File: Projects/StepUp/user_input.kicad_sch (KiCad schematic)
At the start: 10 parts, among them J12 Conn_02x03_Odd_Even

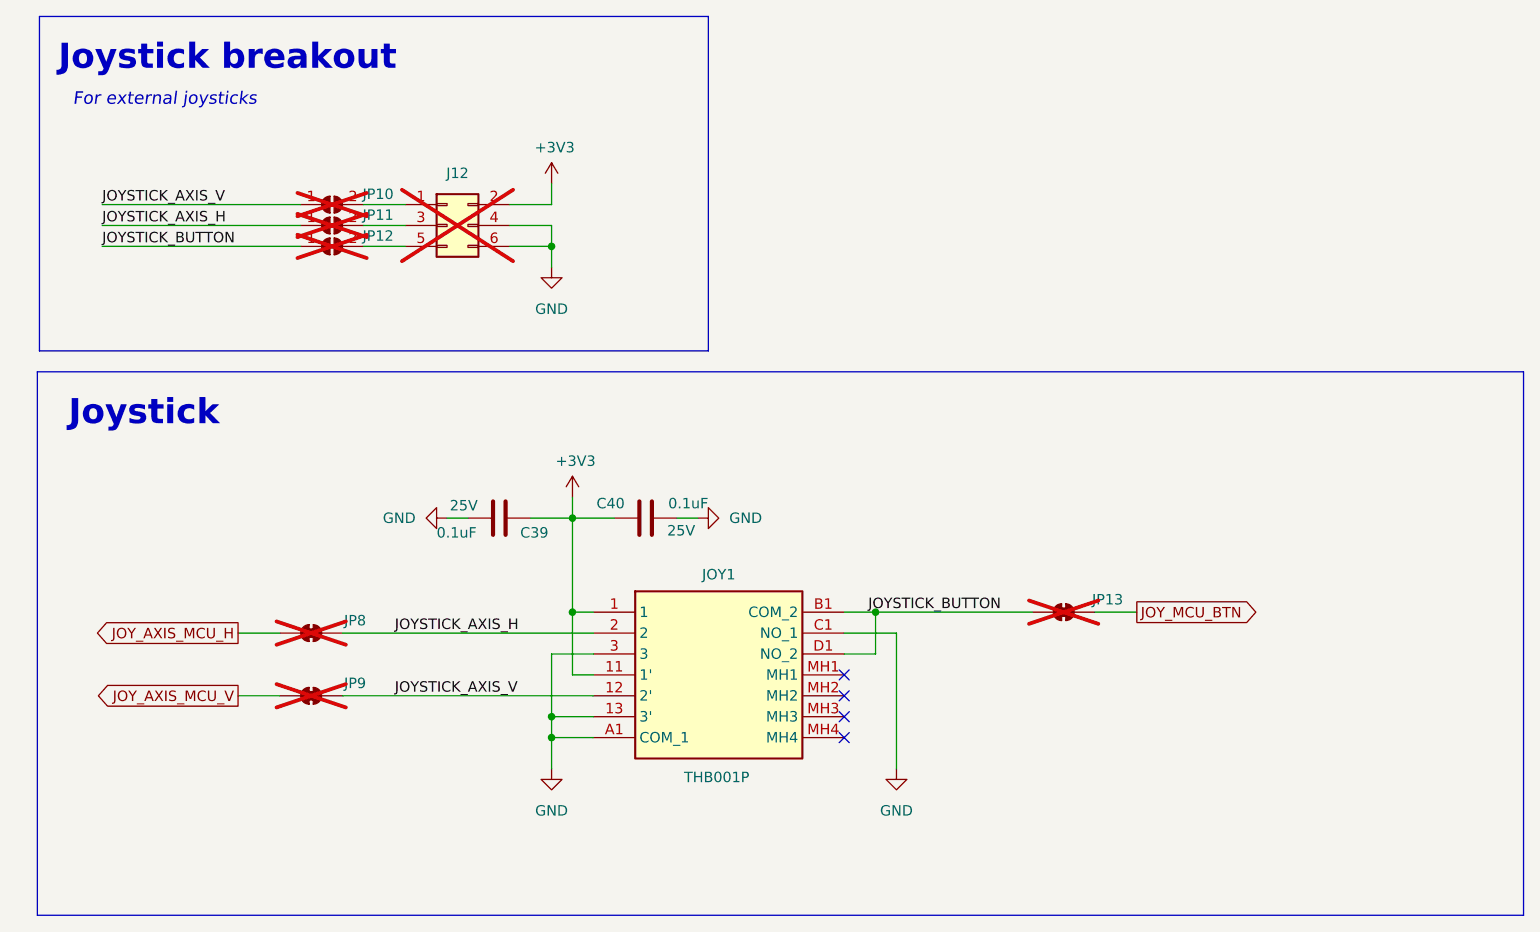
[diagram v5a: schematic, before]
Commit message: feat(v0.2): Schematic updated, PCB layout start
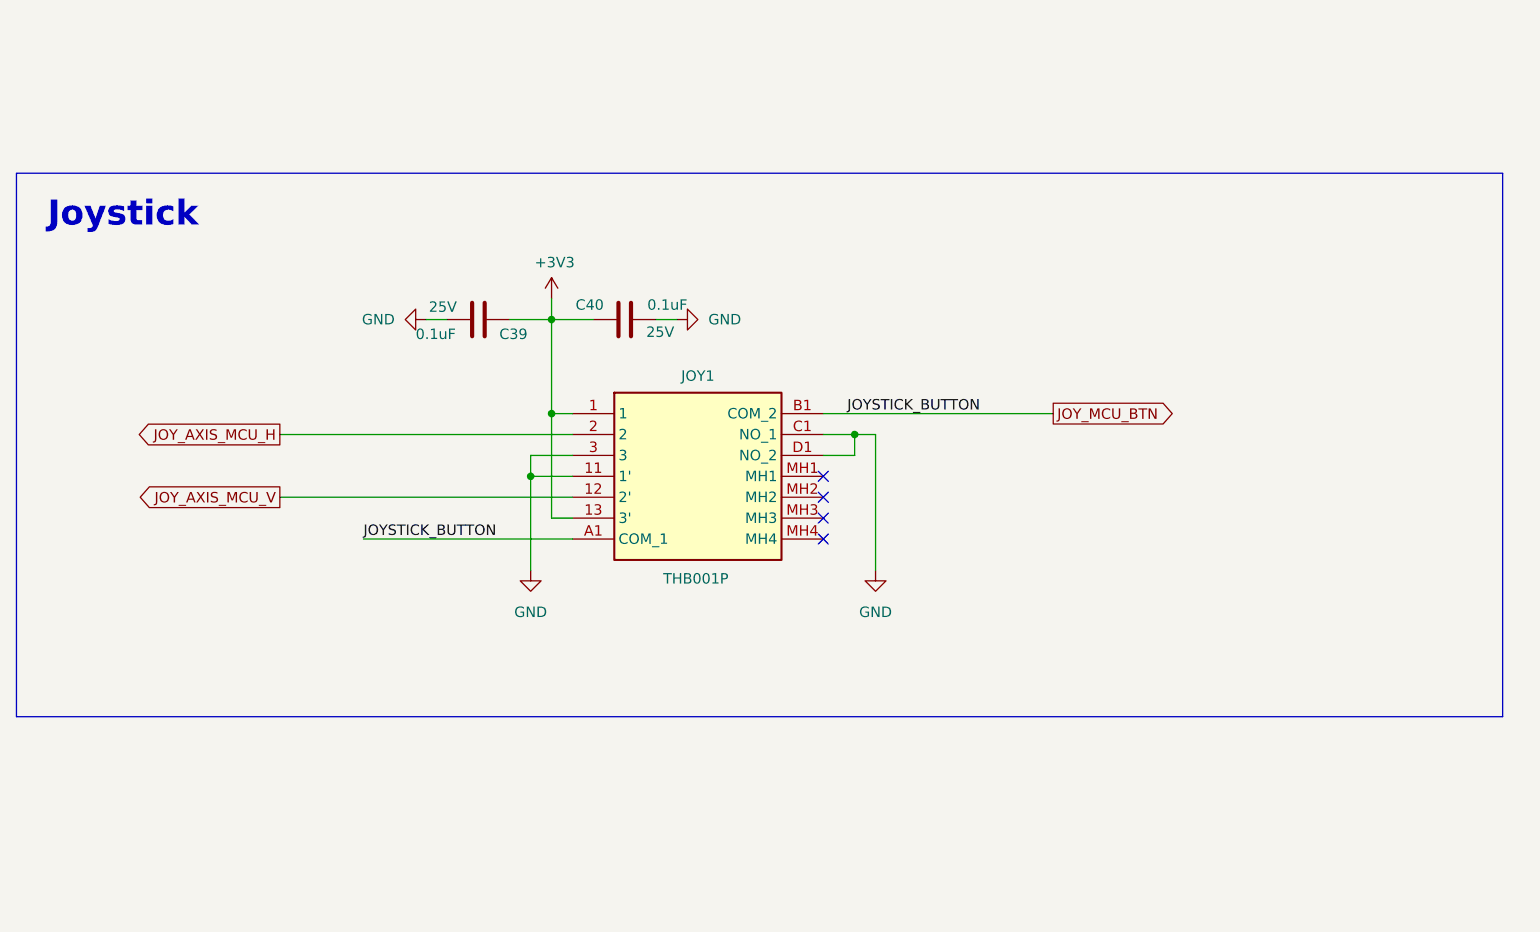
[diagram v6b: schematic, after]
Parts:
- removed J12: Conn_02x03_Odd_Even, Connector_PinHeader_2.54mm:PinHeader_2x03_P2.54mm_Vertical, symbol Connector_Generic:Conn_02x03_Odd_Even
- removed JP10, JP11, JP12: SolderJumper_2_Open, Jumper:SolderJumper-2_P1.3mm_Open_RoundedPad1.0x1.5mm, symbol Jumper:SolderJumper_2_Open
- removed JP13, JP8, JP9: SolderJumper_2_Bridged, Jumper:SolderJumper-2_P1.3mm_Bridged2Bar_RoundedPad1.0x1.5mm, symbol Jumper:SolderJumper_2_Bridged
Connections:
- net JOYSTICK_AXIS_H is gone; now on net JOY_AXIS_MCU_H: JOY1.2
- net JOYSTICK_AXIS_V is gone; now on net JOY_AXIS_MCU_V: JOY1.12 (2')
- net +3V3: now also JOY1.13 (3'); no longer JOY1.11 (1')
- net GND: now also JOY1.11 (1'), JOY1.D1 (NO_2); no longer JOY1.13 (3'), JOY1.A1 (COM_1)
- net JOY_MCU_BTN: now also JOY1.A1 (COM_1), JOY1.B1 (COM_2)
- removed net JOYSTICK_BUTTON: JOY1.B1 (COM_2), JOY1.D1 (NO_2)
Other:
- note removed: "For external joysticks"
- note removed: "Joystick breakout"
- moved on the sheet: C39, C40, JOY1

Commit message: feat(v0.2): Rough layout begins
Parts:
- renumbered C39 to C40, C40 to C41

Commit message: feat(v0.2): Component layout from CAD
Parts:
- JOY1: now left out of the parts list
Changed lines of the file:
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@@
 		(unit 1)
 		(exclude_from_sim no)
-		(in_bom yes)
+		(in_bom no)
 		(on_board yes)
 		(dnp no)
